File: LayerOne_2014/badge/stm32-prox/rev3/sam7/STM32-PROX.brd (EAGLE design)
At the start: 99 x 50 mm, 273 parts, among them IC10 74XX244, IC105 MCP1824T-250, IC106 MCP1824T-120, IC11 CD4066, IC12 AT91SAM7S64, IC13 PQ1X331M2ZP-3V3-LDO-SOT-23-5, IC14 AD8052, IC3 PQ1X331M2ZP-3V3-LDO-SOT-23-5, IC4 HCU-INVERTER, IC5 TLV3502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

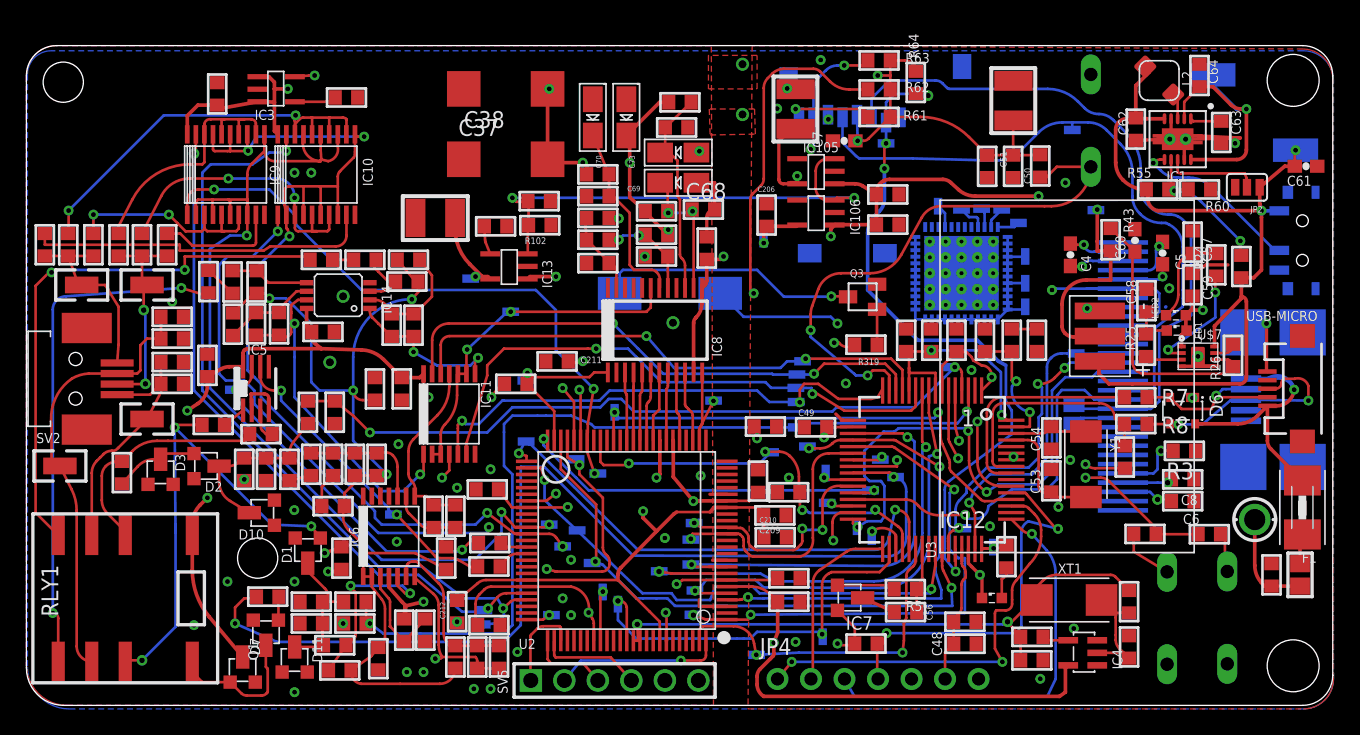
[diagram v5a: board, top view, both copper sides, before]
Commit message: Beefed up power tidied up routes
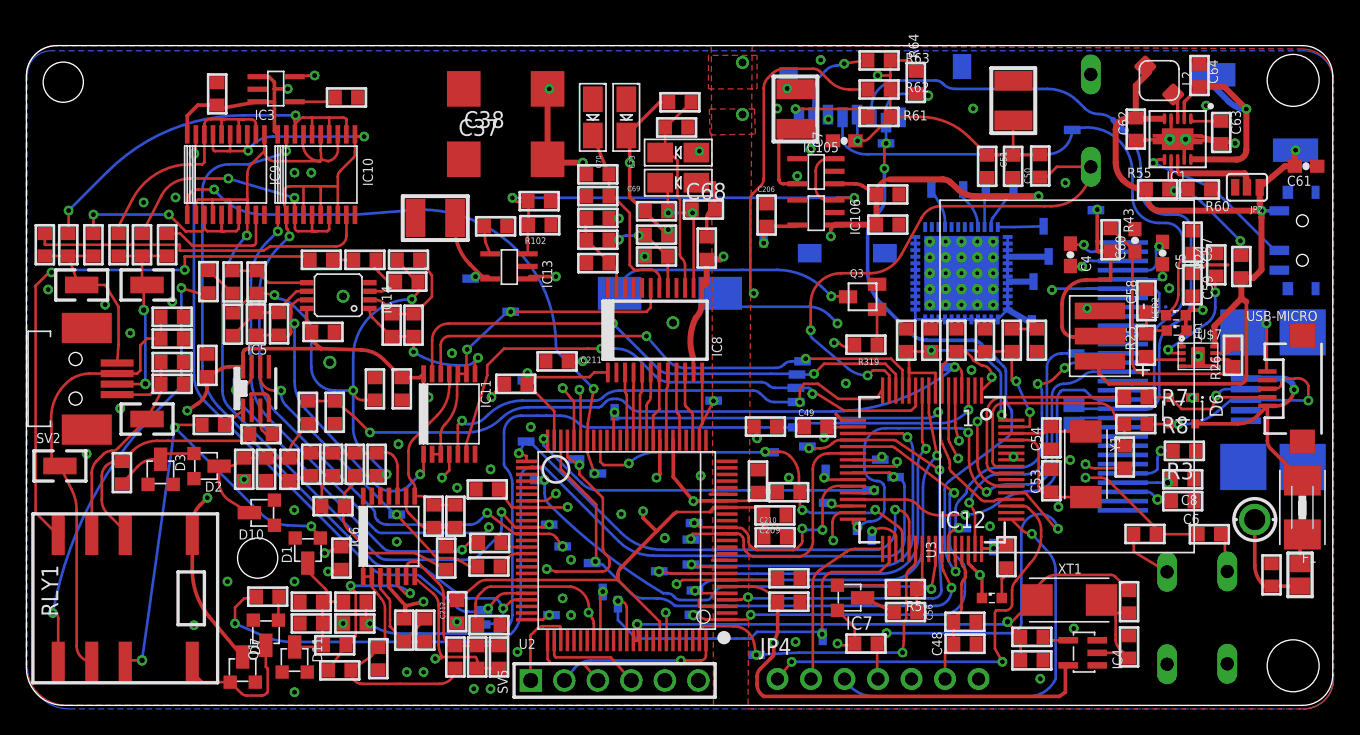
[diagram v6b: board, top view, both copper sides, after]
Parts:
- moved TP25 4.82 mm to (38.8, 16.1), turned to 180 degrees
- moved TP12 1.92 mm to (77.1, 35.3), turned to 270 degrees
- moved TP56 1.78 mm to (77.5, 33.0)
- moved TP13 1.76 mm to (74.8, 38.1), turned to 270 degrees
- moved TP15 1.53 mm to (71.0, 38.1), turned to 270 degrees
- moved TP14 1.49 mm to (72.7, 38.1), turned to 90 degrees
- moved TP43 1.37 mm to (76.2, 27.9)
- moved TP42 1.37 mm to (68.6, 38.1)
- moved TP44 0.65 mm to (76.3, 31.1)
- moved OE6 0.36 mm to (15.9, 23.2), turned to 90 degrees
- moved OE5 0.25 mm to (28.1, 13.5)
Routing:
- net B_RLY_NO: track 39.5 -> 33.6 mm
- net +3V3: track 254.6 -> 260.0 mm
- net PWR_OE2: track 64.1 -> 58.9 mm
- net SCLK_OLED_SD: track 79.0 -> 75.3 mm
- net VDD_0V9: track 46.4 -> 49.6 mm
- net +3V3-FPGA: track 164.2 -> 161.3 mm
- net +1V2: track 79.3 -> 76.8 mm
- net PWR_HI: track 77.8 -> 75.4 mm
- net PWR_OE1: track 48.0 -> 45.9 mm
- net VBUS_IN: track 21.1 -> 19.1 mm
- net +2V5: track 93.3 -> 91.4 mm
- net PWR_LO: track 77.7 -> 75.9 mm
- net INCLK: track 1.70 -> 3.47 mm
- net INSCK: track 1.66 -> 3.38 mm
- net B_RLY_NC: track 37.3 -> 35.6 mm
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
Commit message: changed battery gnd routing changed 90o angles on arkos notes.
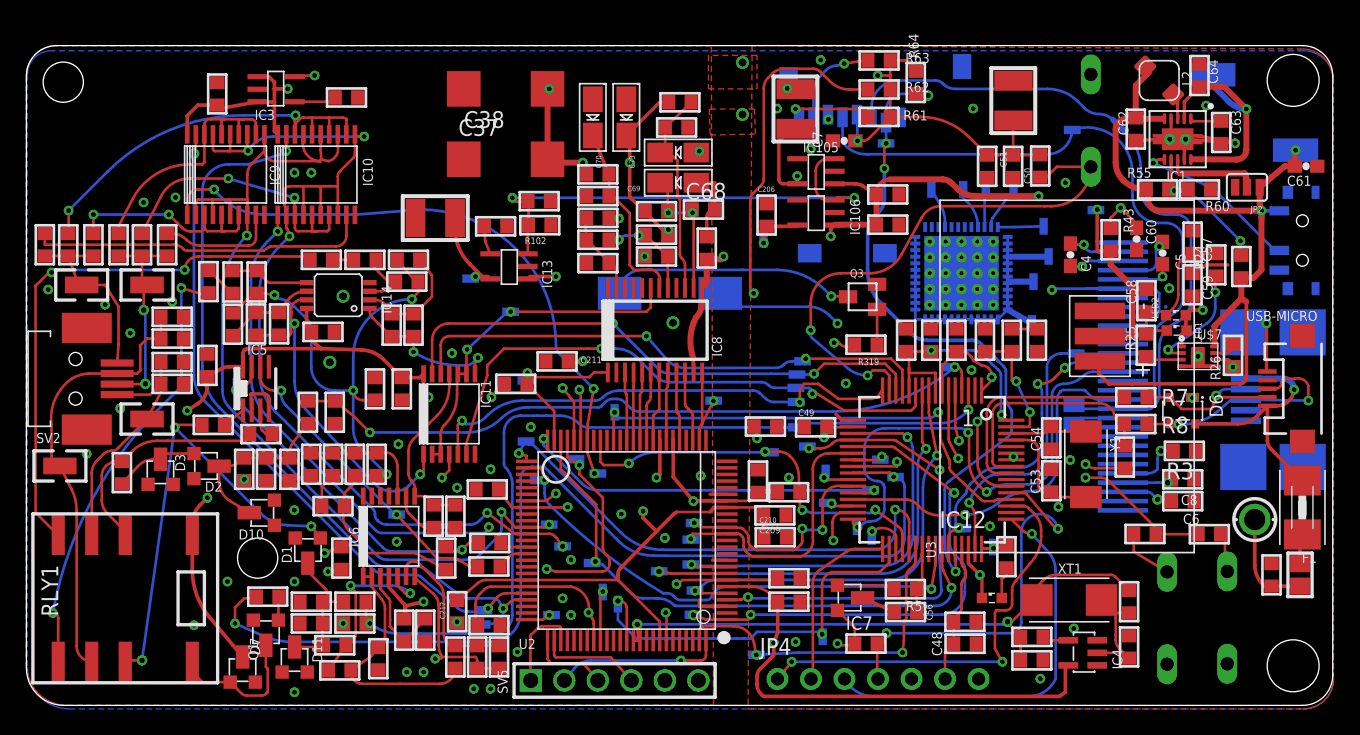
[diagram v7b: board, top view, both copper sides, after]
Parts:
- moved C60 0.16 mm to (84.1, 34.3), turned to 270 degrees
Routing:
- net N$65: track 21.5 -> 26.9 mm, vias 0 -> 2
- net NTC: track 15.9 -> 14.0 mm
- net A_RLY_NO: track 42.0 -> 41.4 mm
- net GND: vias 66 -> 65

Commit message: silk updated test points moved
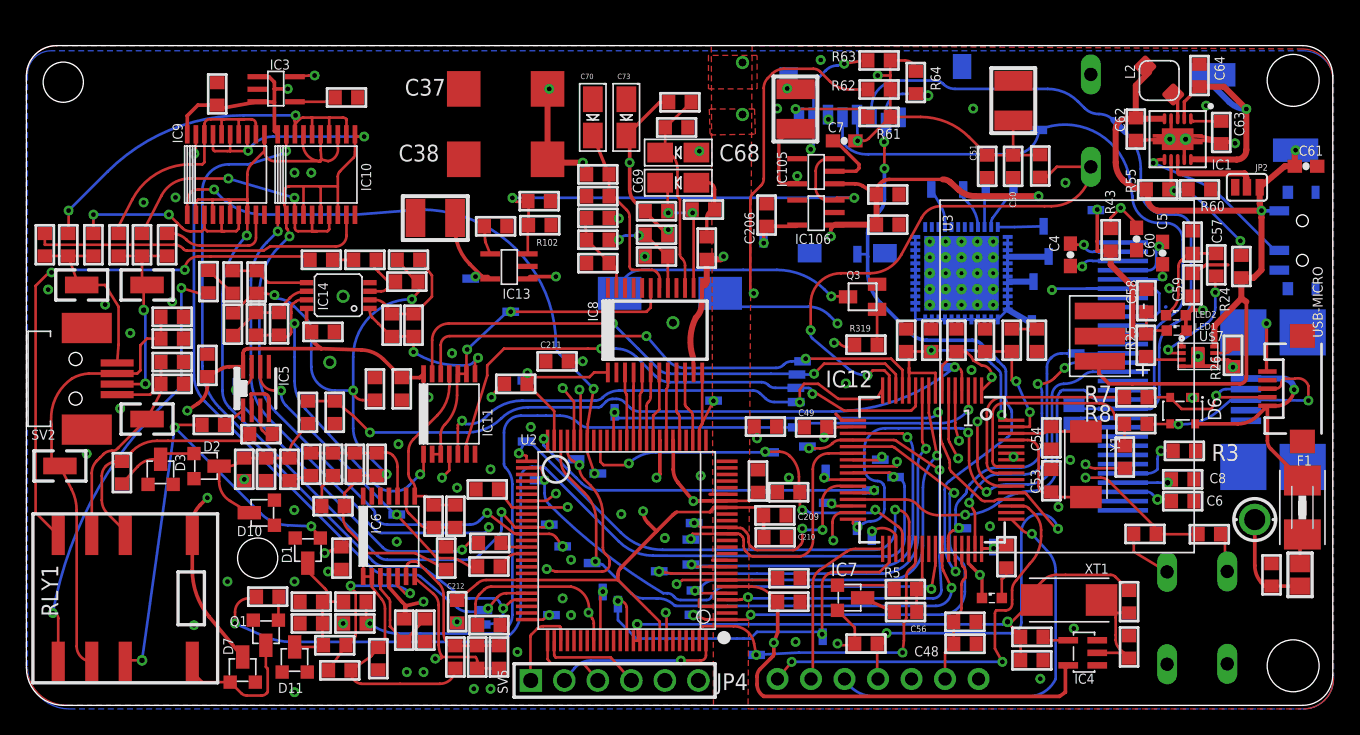
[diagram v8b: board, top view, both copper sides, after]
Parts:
- moved TP7 8.68 mm to (63.0, 33.2), turned to 90 degrees
- moved TP54 2.54 mm to (76.7, 42.6)
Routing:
- net GND: track 51.6 -> 56.2 mm
- net !CS_SD: track 51.2 -> 52.7 mm
- net SCLK_OLED_SD: track 75.3 -> 74.4 mm
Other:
- board text added: "charlie@x.io"
- board text added: "rev6"
